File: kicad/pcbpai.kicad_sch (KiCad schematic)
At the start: 20 parts, among them J1 Fuse, J10 Conn_01x02_Socket, J11 Conn_01x02_Socket, J12 Conn_01x02_Socket, J2 Conn_01x08_Socket, J3 Input 24 V, J4 Boton Encendido, J5 Parada de Emergencia, J6 Conn_01x08_Socket, J7 Raspberry GPIO, J8 Conn_01x02_Socket, J9 Conn_01x02_Socket, U6 ATtiny85-20P

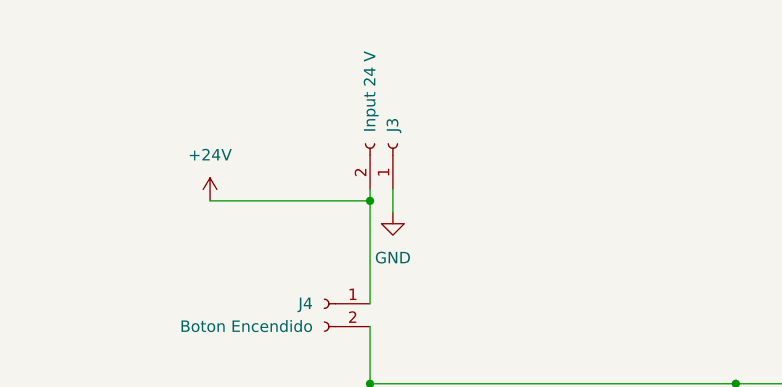
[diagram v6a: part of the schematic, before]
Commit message: fix xt60 polarity
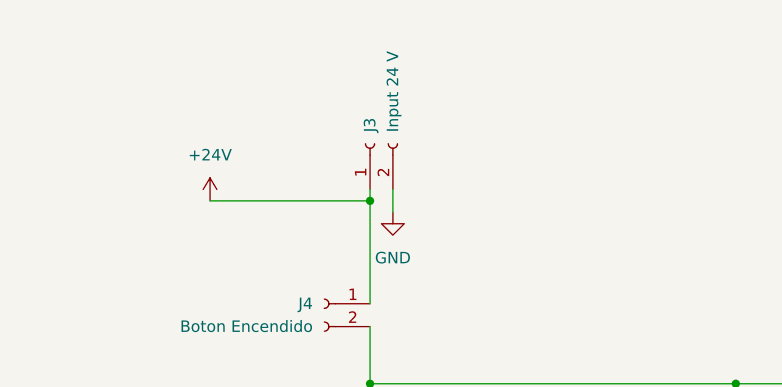
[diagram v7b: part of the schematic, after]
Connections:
- net +24V: now also J3.1 (Pin_1); no longer J3.2 (Pin_2)
- net GND: now also J3.2 (Pin_2); no longer J3.1 (Pin_1)
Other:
- moved on the sheet: J3
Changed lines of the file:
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@@
+    (stroke (width 0) (type default))
+  )
+  (wire (pts (xy 222.25 146.05) (xy 204.47 146.05))
+    (stroke (width 0) (type default))
+  )
+  (wire (pts (xy 165.1 138.43) (xy 167.64 138.43))
+    (stroke (width 0) (type default))
+  )
+  (wire (pts (xy 165.1 123.19) (xy 167.64 123.19))
+    (stroke (width 0) (type default))
+  )
+  (wire (pts (xy 132.08 118.11) (xy 167.64 118.11))
+    (stroke (width 0) (type default))
+  )
+  (wire (pts (xy 149.86 143.51) (xy 149.86 140.97))
+    (stroke (width 0) (type default))
+  )
+  (wire (pts (xy 167.64 81.28) (xy 167.64 102.87))
+    (stroke (width 0) (type default))
+  )
+  (wire (pts (xy 165.1 130.81) (xy 167.64 130.81))
+    (stroke (width 0) (type default))
+  )
+  (wire (pts (xy 180.34 135.89) (xy 184.15 135.89))
+    (stroke (width 0) (type default))
+  )
+  (wire (pts (xy 222.25 143.51) (xy 222.25 146.05))
+    (stroke (width 0) (type default))
+  )
+  (wire (pts (xy 165.1 125.73) (xy 167.64 125.73))
+    (stroke (width 0) (type default))
+  )
+  (wire (pts (xy 154.94 96.52) (xy 154.94 107.95))
+    (stroke (width 0) (type default))
+  )
+  (wire (pts (xy 154.94 50.8) (xy 154.94 41.91))
     (stroke (width 0) (type default))
   )
   (wire (pts (xy 83.82 34.29) (xy 83.82 36.83))
-    (stroke (width 0) (type default))
-  )
-  (wire (pts (xy 222.25 146.05) (xy 204.47 146.05))
-    (stroke (width 0) (type default))
-  )
-  (wire (pts (xy 165.1 138.43) (xy 167.64 138.43))
-    (stroke (width 0) (type default))
-  )
-  (wire (pts (xy 165.1 123.19) (xy 167.64 123.19))
-    (stroke (width 0) (type default))
-  )
-  (wire (pts (xy 132.08 118.11) (xy 167.64 118.11))
-    (stroke (width 0) (type default))
-  )
-  (wire (pts (xy 149.86 143.51) (xy 149.86 140.97))
-    (stroke (width 0) (type default))
-  )
-  (wire (pts (xy 167.64 81.28) (xy 167.64 102.87))
-    (stroke (width 0) (type default))
-  )
-  (wire (pts (xy 165.1 130.81) (xy 167.64 130.81))
-    (stroke (width 0) (type default))
-  )
-  (wire (pts (xy 180.34 135.89) (xy 184.15 135.89))
-    (stroke (width 0) (type default))
-  )
-  (wire (pts (xy 222.25 143.51) (xy 222.25 146.05))
-    (stroke (width 0) (type default))
-  )
-  (wire (pts (xy 165.1 125.73) (xy 167.64 125.73))
-    (stroke (width 0) (type default))
-  )
-  (wire (pts (xy 154.94 96.52) (xy 154.94 107.95))
-    (stroke (width 0) (type default))
-  )
-  (wire (pts (xy 154.94 50.8) (xy 154.94 41.91))
     (stroke (width 0) (type default))
   )
@@
     )
   )
-  (symbol (lib_id "Connector:Conn_01x02_Socket") (at 83.82 29.21 270) (mirror x) (unit 1)
+  (symbol (lib_id "Connector:Conn_01x02_Socket") (at 81.28 29.21 90) (unit 1)
     (in_bom yes) (on_board yes) (dnp no)
-    (property "Reference" "J3" (at 83.82 27.94 0)
-      (effects (font (size 1.27 1.27)) (justify left))
-    )
-    (property "Value" "Input 24 V" (at 81.28 27.94 0)
-      (effects (font (size 1.27 1.27)) (justify left))
-    )
-    (property "Footprint" "Connector_AMASS:AMASS_XT60-M_1x02_P7.20mm_Vertical" (at 83.82 29.21 0)
-      (effects (font (size 1.27 1.27)) hide)
-    )
-    (property "Datasheet" "~" (at 83.82 29.21 0)
-      (effects (font (size 1.27 1.27)) hide)
-    )
+    (property "Reference" "J3" (at 81.28 27.94 0)
+      (effects (font (size 1.27 1.27)) (justify left))
+    )
+    (property "Value" "Input 24 V" (at 83.82 27.94 0)
+      (effects (font (size 1.27 1.27)) (justify left))
+    )
+    (property "Footprint" "Connector_AMASS:AMASS_XT60-M_1x02_P7.20mm_Vertical" (at 81.28 29.21 0)
+      (effects (font (size 1.27 1.27)) hide)
+    )
+    (property "Datasheet" "~" (at 81.28 29.21 0)
+      (effects (font (size 1.27 1.27)) hide)
+    )

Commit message: unfix xt60 polarity
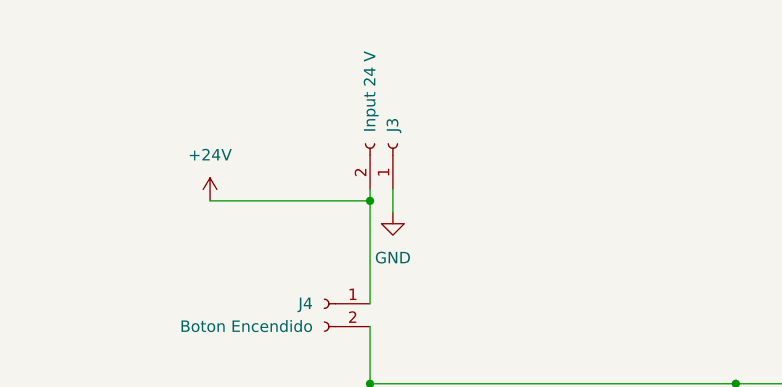
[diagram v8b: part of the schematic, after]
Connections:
- net +24V: now also J3.2 (Pin_2); no longer J3.1 (Pin_1)
- net GND: now also J3.1 (Pin_1); no longer J3.2 (Pin_2)
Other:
- moved on the sheet: J3
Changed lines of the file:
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@@
     (company "Universidad Nacional de Colombia")
   )
+  (junction (at 81.28 35.56) (diameter 0) (color 0 0 0 0)
+  )
   (junction (at 83.82 90.17) (diameter 0) (color 0 0 0 0)
   )
@@
   )
   (junction (at 149.86 115.57) (diameter 0) (color 0 0 0 0)
-  )
-  (junction (at 81.28 35.56) (diameter 0) (color 0 0 0 0)
   )
   (junction (at 167.64 81.28) (diameter 0) (color 0 0 0 0)
@@
     (stroke (width 0) (type default))
   )
+  (wire (pts (xy 182.88 115.57) (xy 180.34 115.57))
+    (stroke (width 0) (type default))
+  )
+  (wire (pts (xy 132.08 41.91) (xy 132.08 50.8))
+    (stroke (width 0) (type default))
+  )
+  (wire (pts (xy 180.34 143.51) (xy 184.15 143.51))
+    (stroke (width 0) (type default))
+  )
+  (wire (pts (xy 180.34 133.35) (xy 184.15 133.35))
+    (stroke (width 0) (type default))
+  )
+  (wire (pts (xy 201.93 134.62) (xy 201.93 132.08))
+    (stroke (width 0) (type default))
+  )
+  (wire (pts (xy 220.98 123.19) (xy 180.34 123.19))
+    (stroke (width 0) (type default))
+  )
+  (wire (pts (xy 149.86 148.59) (xy 167.64 148.59))
+    (stroke (width 0) (type default))
+  )
+  (wire (pts (xy 222.25 151.13) (xy 180.34 151.13))
+    (stroke (width 0) (type default))
+  )
+  (wire (pts (xy 121.92 71.12) (xy 121.92 73.66))
+    (stroke (width 0) (type default))
+  )
+  (wire (pts (xy 182.88 118.11) (xy 182.88 115.57))
+    (stroke (width 0) (type default))
+  )
+  (wire (pts (xy 199.39 106.68) (xy 199.39 104.14))
+    (stroke (width 0) (type default))
+  )
+  (wire (pts (xy 180.34 138.43) (xy 184.15 138.43))
+    (stroke (width 0) (type default))
+  )
+  (wire (pts (xy 69.85 92.71) (xy 72.39 92.71))
+    (stroke (width 0) (type default))
+  )
+  (wire (pts (xy 129.54 97.79) (xy 152.4 97.79))
+    (stroke (width 0) (type default))
+  )
+  (wire (pts (xy 132.08 113.03) (xy 149.86 113.03))
+    (stroke (width 0) (type default))
+  )
+  (wire (pts (xy 203.2 118.11) (xy 182.88 118.11))
+    (stroke (width 0) (type default))
+  )
+  (wire (pts (xy 180.34 130.81) (xy 184.15 130.81))
+    (stroke (width 0) (type default))
+  )
+  (wire (pts (xy 154.94 55.88) (xy 162.56 55.88))
+    (stroke (width 0) (type default))
+  )
+  (wire (pts (xy 129.54 97.79) (xy 129.54 71.12))
+    (stroke (width 0) (type default))
+  )
+  (wire (pts (xy 132.08 134.62) (xy 129.54 134.62))
+    (stroke (width 0) (type default))
+  )
+  (wire (pts (xy 81.28 55.88) (xy 121.92 55.88))
+    (stroke (width 0) (type default))
+  )
+  (wire (pts (xy 180.34 120.65) (xy 203.2 120.65))
+    (stroke (width 0) (type default))
+  )
+  (wire (pts (xy 149.86 143.51) (xy 167.64 143.51))
+    (stroke (width 0) (type default))
+  )
+  (wire (pts (xy 83.82 92.71) (xy 96.52 92.71))
+    (stroke (width 0) (type default))
+  )
+  (wire (pts (xy 132.08 120.65) (xy 132.08 118.11))
+    (stroke (width 0) (type default))
+  )
+  (wire (pts (xy 121.92 55.88) (xy 132.08 55.88))
+    (stroke (width 0) (type default))
+  )
+  (wire (pts (xy 149.86 115.57) (xy 149.86 113.03))
+    (stroke (width 0) (type default))
+  )
+  (wire (pts (xy 81.28 34.29) (xy 81.28 35.56))
+    (stroke (width 0) (type default))
+  )
   (wire (pts (xy 83.82 34.29) (xy 83.82 36.83))
     (stroke (width 0) (type default))
   )
-  (wire (pts (xy 182.88 115.57) (xy 180.34 115.57))
-    (stroke (width 0) (type default))
-  )
-  (wire (pts (xy 132.08 41.91) (xy 132.08 50.8))
-    (stroke (width 0) (type default))
-  )
-  (wire (pts (xy 180.34 143.51) (xy 184.15 143.51))
-    (stroke (width 0) (type default))
-  )
-  (wire (pts (xy 180.34 133.35) (xy 184.15 133.35))
-    (stroke (width 0) (type default))
-  )
-  (wire (pts (xy 201.93 134.62) (xy 201.93 132.08))
-    (stroke (width 0) (type default))
-  )
-  (wire (pts (xy 220.98 123.19) (xy 180.34 123.19))
-    (stroke (width 0) (type default))
-  )
-  (wire (pts (xy 149.86 148.59) (xy 167.64 148.59))
-    (stroke (width 0) (type default))
-  )
-  (wire (pts (xy 222.25 151.13) (xy 180.34 151.13))
-    (stroke (width 0) (type default))
-  )
-  (wire (pts (xy 121.92 71.12) (xy 121.92 73.66))
-    (stroke (width 0) (type default))
-  )
-  (wire (pts (xy 182.88 118.11) (xy 182.88 115.57))
-    (stroke (width 0) (type default))
-  )
-  (wire (pts (xy 199.39 106.68) (xy 199.39 104.14))
-    (stroke (width 0) (type default))
-  )
-  (wire (pts (xy 180.34 138.43) (xy 184.15 138.43))
-    (stroke (width 0) (type default))
-  )
-  (wire (pts (xy 69.85 92.71) (xy 72.39 92.71))
-    (stroke (width 0) (type default))
-  )
-  (wire (pts (xy 129.54 97.79) (xy 152.4 97.79))
-    (stroke (width 0) (type default))
-  )
-  (wire (pts (xy 132.08 113.03) (xy 149.86 113.03))
-    (stroke (width 0) (type default))
-  )
-  (wire (pts (xy 203.2 118.11) (xy 182.88 118.11))
-    (stroke (width 0) (type default))
-  )
-  (wire (pts (xy 180.34 130.81) (xy 184.15 130.81))
-    (stroke (width 0) (type default))
-  )
-  (wire (pts (xy 154.94 55.88) (xy 162.56 55.88))
-    (stroke (width 0) (type default))
-  )
-  (wire (pts (xy 129.54 97.79) (xy 129.54 71.12))
-    (stroke (width 0) (type default))
-  )
-  (wire (pts (xy 132.08 134.62) (xy 129.54 134.62))
-    (stroke (width 0) (type default))
-  )
-  (wire (pts (xy 81.28 55.88) (xy 121.92 55.88))
-    (stroke (width 0) (type default))
-  )
-  (wire (pts (xy 180.34 120.65) (xy 203.2 120.65))
-    (stroke (width 0) (type default))
-  )
-  (wire (pts (xy 149.86 143.51) (xy 167.64 143.51))
-    (stroke (width 0) (type default))
-  )
-  (wire (pts (xy 83.82 92.71) (xy 96.52 92.71))
-    (stroke (width 0) (type default))
-  )
-  (wire (pts (xy 132.08 120.65) (xy 132.08 118.11))
-    (stroke (width 0) (type default))
-  )
-  (wire (pts (xy 121.92 55.88) (xy 132.08 55.88))
-    (stroke (width 0) (type default))
-  )
-  (wire (pts (xy 149.86 115.57) (xy 149.86 113.03))
-    (stroke (width 0) (type default))
-  )
   (wire (pts (xy 165.1 128.27) (xy 167.64 128.27))
     (stroke (width 0) (type default))
@@
   )
   (wire (pts (xy 83.82 92.71) (xy 83.82 99.06))
-    (stroke (width 0) (type default))
-  )
-  (wire (pts (xy 81.28 34.29) (xy 81.28 35.56))
     (stroke (width 0) (type default))
   )
@@
     )
   )
-  (symbol (lib_id "Connector:Conn_01x02_Socket") (at 81.28 29.21 90) (unit 1)
+  (symbol (lib_id "Connector:Conn_01x02_Socket") (at 83.82 29.21 270) (mirror x) (unit 1)
     (in_bom yes) (on_board yes) (dnp no)
-    (property "Reference" "J3" (at 81.28 27.94 0)
-      (effects (font (size 1.27 1.27)) (justify left))
-    )
-    (property "Value" "Input 24 V" (at 83.82 27.94 0)
-      (effects (font (size 1.27 1.27)) (justify left))
-    )
-    (property "Footprint" "Connector_AMASS:AMASS_XT60-M_1x02_P7.20mm_Vertical" (at 81.28 29.21 0)
-      (effects (font (size 1.27 1.27)) hide)
-    )
-    (property "Datasheet" "~" (at 81.28 29.21 0)
-      (effects (font (size 1.27 1.27)) hide)
-    )
+    (property "Reference" "J3" (at 83.82 27.94 0)
+      (effects (font (size 1.27 1.27)) (justify left))
+    )
+    (property "Value" "Input 24 V" (at 81.28 27.94 0)
+      (effects (font (size 1.27 1.27)) (justify left))
+    )
+    (property "Footprint" "Connector_AMASS:AMASS_XT60-M_1x02_P7.20mm_Vertical" (at 83.82 29.21 0)
+      (effects (font (size 1.27 1.27)) hide)
+    )
+    (property "Datasheet" "~" (at 83.82 29.21 0)
+      (effects (font (size 1.27 1.27)) hide)
+    )
